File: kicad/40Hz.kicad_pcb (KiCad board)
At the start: 2 copper layers, 78.7 x 58.4 mm, 30 parts, among them J1 Screw_Terminal_01x06, J2 5V, J3 SSD1306, Q1 IRF540N, SW1 CANC, SW2 UP, SW3 DOWN, SW4 ENT, U1 ESP-12F, U2 WeMos_D1_mini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

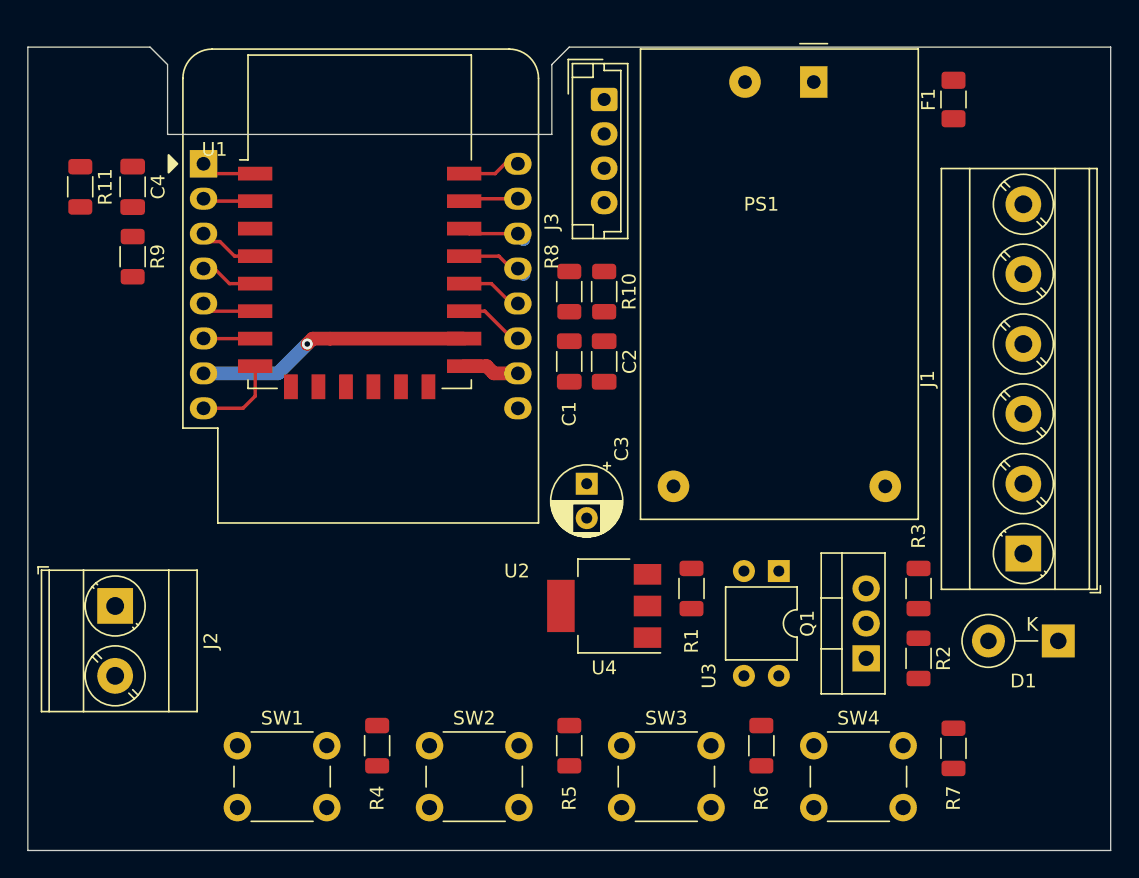
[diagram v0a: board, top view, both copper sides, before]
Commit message: Add CRC Check on Settings
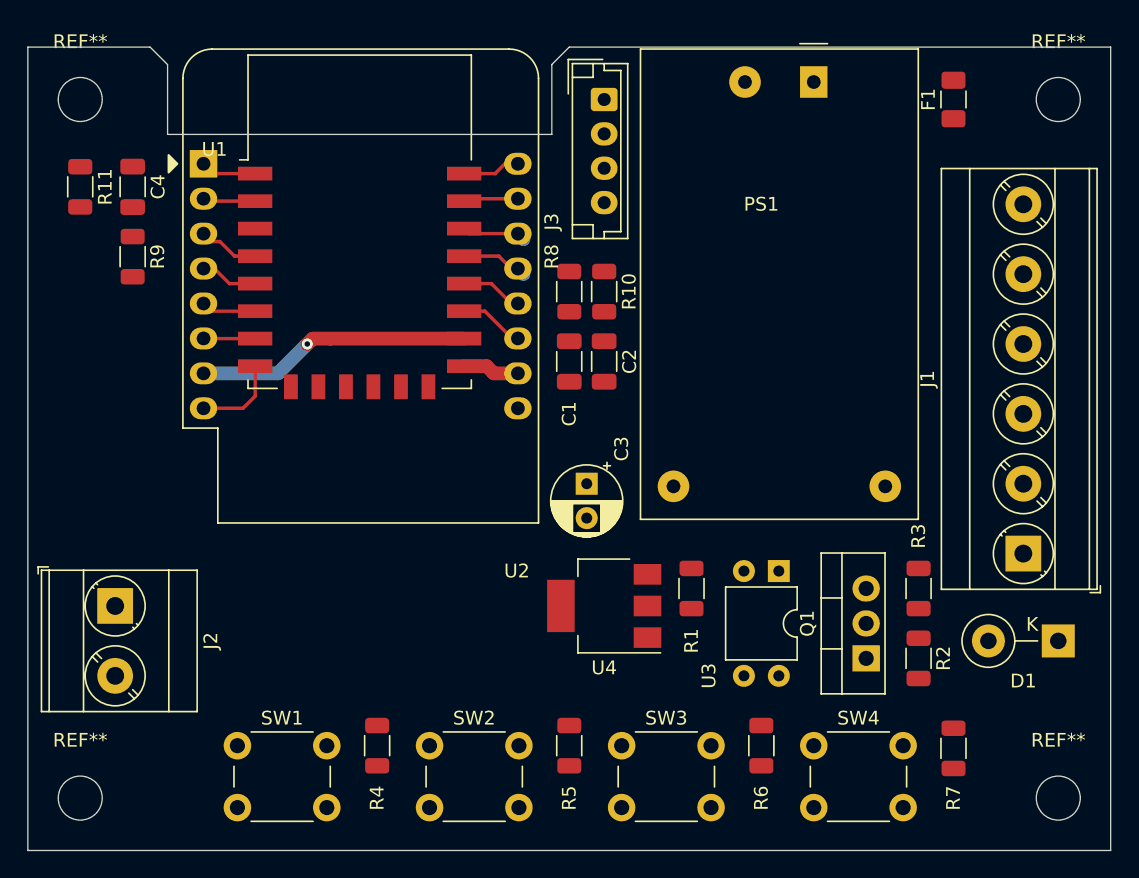
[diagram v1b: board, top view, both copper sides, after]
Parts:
- added REF**: MountingHole_3.2mm_M3, MountingHole:MountingHole_3.2mm_M3, F.Cu at (268.0, 124.5)
- added REF**: MountingHole_3.2mm_M3, MountingHole:MountingHole_3.2mm_M3, F.Cu at (196.8, 124.5)
- added REF**: MountingHole_3.2mm_M3, MountingHole:MountingHole_3.2mm_M3, F.Cu at (196.8, 73.7)
- added REF**: MountingHole_3.2mm_M3, MountingHole:MountingHole_3.2mm_M3, F.Cu at (268.0, 73.7)

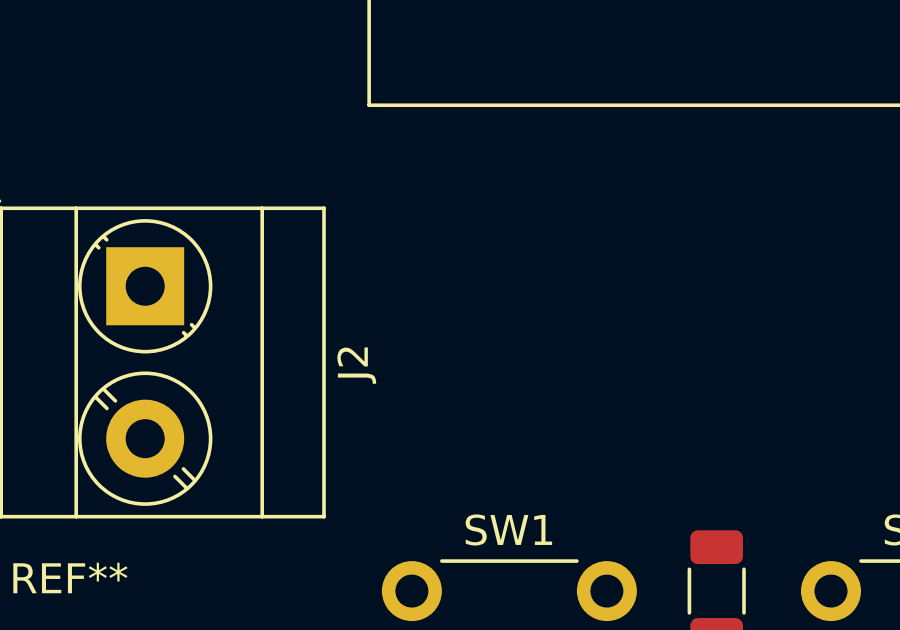
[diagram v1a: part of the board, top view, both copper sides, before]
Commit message: Fuse added
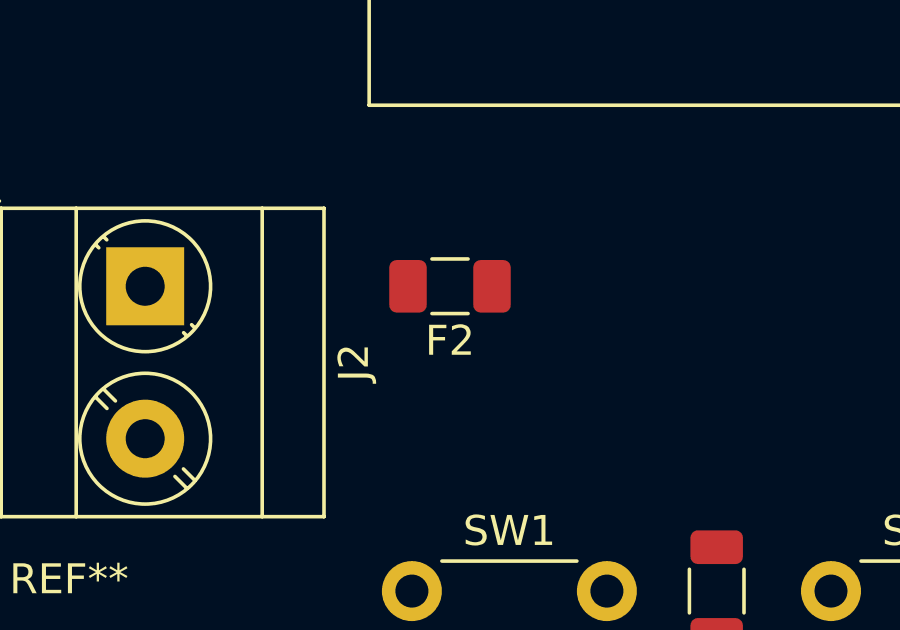
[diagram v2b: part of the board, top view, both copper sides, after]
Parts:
- added F2: 200mA, Fuse:Fuse_1206_3216Metric, F.Cu at (209.6, 110.5)
- C1, C2, C4: value C -> 100n
- C3: value CP -> 10uF
- F1: value 200mA -> 100mA
- J1: value Screw_Terminal_01x06 -> Power
- R1: value R -> 470
- R10, R11, R3, R4, R5, R6, R7, R8, R9: value R -> 10k
- R2: value R -> 220
- SW1: value CANC -> OK
- SW4: value ENT -> CANC
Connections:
- J2 pad 1: +5V -> Net-(F2-Pad2)
- R4 pad 1: /IO16 -> /IO14
- R5 pad 1: /IO14 -> /IO16
- SW1 pad 1: /IO16 -> /IO14
- SW2 pad 1: /IO14 -> /IO16

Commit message: Button alpha
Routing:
- net /IO15: track 20.0 -> 0.00 mm, vias 1 -> 0

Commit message: Release
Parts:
- removed R4, R5, R6, R7: 10k, Resistor_SMD:R_1206_3216Metric
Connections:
- SW1 pad 2: +3V3 -> GND
- SW2 pad 2: +3V3 -> GND
- SW3 pad 2: +3V3 -> GND
- SW4 pad 2: +3V3 -> GND

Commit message: Schematic update
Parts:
- added D2: LED, LED_SMD:LED_1206_3216Metric_Pad1.42x1.75mm_HandSolder, F.Cu at (243.8, 115.6)
- added R4: 10k, Resistor_SMD:R_1206_3216Metric, F.Cu at (247.7, 110.5)
- added R5: 4.7k, Resistor_SMD:R_1206_3216Metric, F.Cu at (247.7, 115.6)
- D1: value BYV79-200 -> 1N4148; footprint Diode_THT:D_DO-15_P5.08mm_Vertical_KathodeUp -> Diode_SMD:D_SOD-123
- J1: footprint TerminalBlock_Phoenix:TerminalBlock_Phoenix_MKDS-3-6-5.08_1x06_P5.08mm_Horizontal -> TerminalBlock_Phoenix:TerminalBlock_Phoenix_MKDS-3-5-5.08_1x05_P5.08mm_Horizontal
- Q1: value IRF540N -> D4184; footprint Package_TO_SOT_THT:TO-220-3_Vertical -> Package_TO_SOT_SMD:TO-252-2
- R2: value 220 -> 4.7k
- R3: value 10k -> 100
- U3: footprint Package_DIP:DIP-4_W7.62mm -> Package_SO:SOP-4_3.8x4.1mm_P2.54mm
- moved D1 23.1 mm to (245.7, 106.7), turned to 0 degrees
- moved U4 23.0 mm to (212.1, 113.0)
- moved R2 17.8 mm to (240.0, 115.6), turned to 90 degrees
- moved R3 14.0 mm to (243.8, 110.5)
- moved U3 8.98 mm to (238.8, 109.2)
- moved R1 7.41 mm to (237.5, 115.6), turned to 270 degrees
- moved F2 3.81 mm to (209.6, 106.7)
- moved C3 2.54 mm to (233.7, 99.1)
- moved Q1 2.54 mm to (254.0, 111.8), turned to 270 degrees
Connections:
- net /RST renamed /\RST
- D1 pad 1: /+IN -> Net-(D1-Pad1)
- D1 pad 2: /-OUT -> /LIGHT_PWR-
- J1 pad 1: /+IN -> /LIGHT_PWR+
- J1 pad 2: /-OUT -> /LIGHT_OUT-
- J1 pad 3: /+IN -> /LIGHT_PWR-
- J1 pad 4: /-IN -> /ACIN1
- J1 pad 5: /ACIN1 -> /ACIN2
- Q1 pad 2: /-OUT -> /LIGHT_OUT-
- Q1 pad 3: /-IN -> /LIGHT_PWR-
- R2 pad 1: /+IN -> /LIGHT_PWR+
- R3 pad 2: /-IN -> Net-(D1-Pad1)
- U3 pad 3: Net-(Q1-Pad1) -> Net-(D1-Pad1)
